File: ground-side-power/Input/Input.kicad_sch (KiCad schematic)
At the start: 35 parts, among them J1 Battery Terminals, J2 Battery Terminals, J3 Battery Terminals, J4 Battery Terminals, J5 455860005, J6 455860005, J7 ATX-24, J8 Conn_01x03_Female, J9 Conn_01x03_Female, K1 AZ2150-1A-12DEF, SW1 GRB234A2NABA1, U1 INA180, U2 INA180

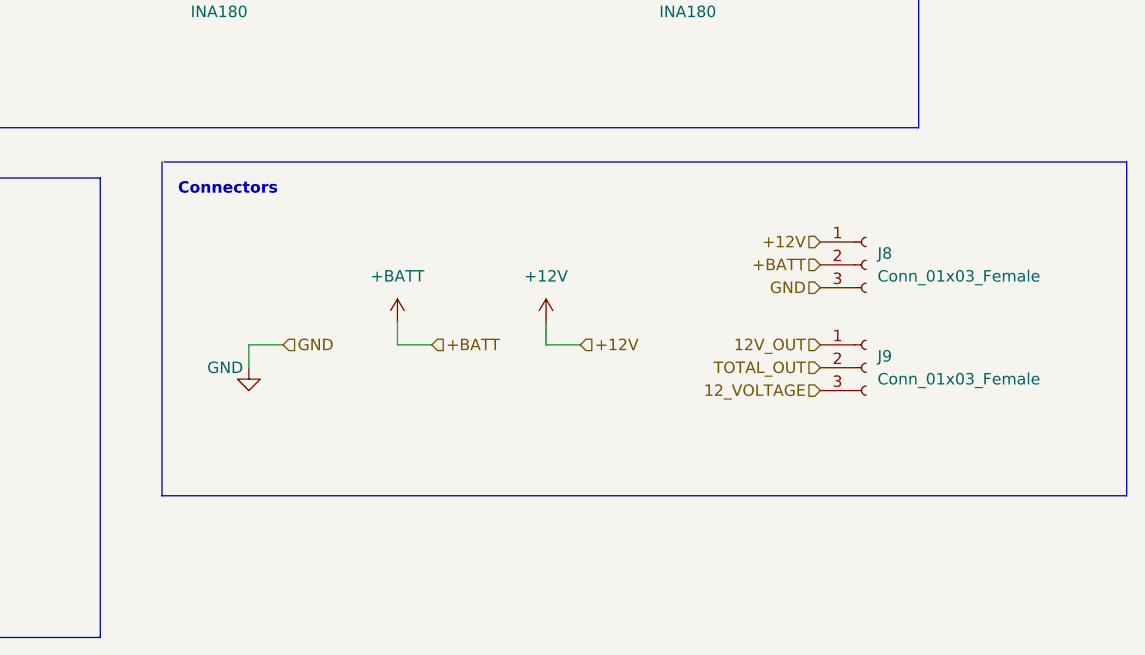
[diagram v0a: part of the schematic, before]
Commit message: Created layout for the footprints for each board
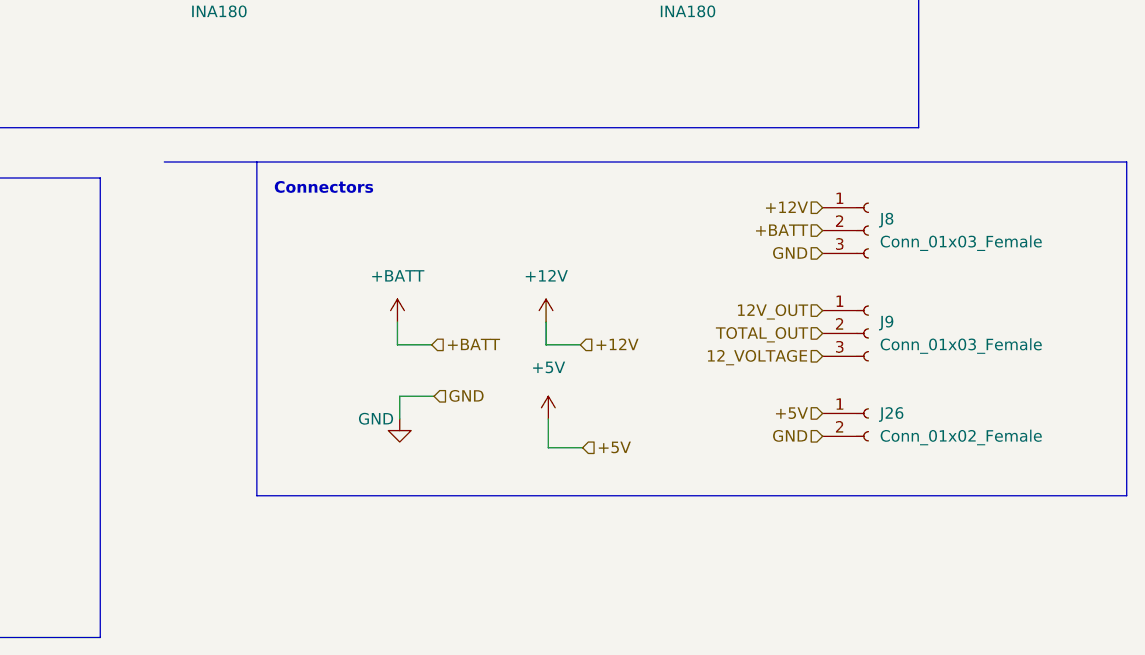
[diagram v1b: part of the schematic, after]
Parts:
- added J26: Conn_01x02_Female, GSP:OSTTA020161, symbol Connector:Conn_01x02_Female
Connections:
- net +5V: now also J26.1 (Pin_1)
- net GND: now also J26.2 (Pin_2)
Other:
- moved on the sheet: J8, J9
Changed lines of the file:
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@@
     (stroke (width 0) (type default) (color 0 0 0 0))
   )
-  (wire (pts (xy 183.896 146.05) (xy 187.706 146.05))
+  (wire (pts (xy 200.66 151.765) (xy 204.47 151.765))
     (stroke (width 0) (type default) (color 0 0 0 0))
   )
@@
     (stroke (width 0) (type default) (color 0 0 0 0))
   )
+  (wire (pts (xy 220.98 157.48) (xy 217.17 157.48))
+    (stroke (width 0) (type default) (color 0 0 0 0))
+  )
   (wire (pts (xy 62.611 31.242) (xy 62.611 32.512))
     (stroke (width 0) (type default) (color 0 0 0 0))
@@
     (stroke (width 0) (type default) (color 0 0 0 0))
   )
-  (polyline (pts (xy 281.432 162.814) (xy 174.244 162.814))
+  (polyline (pts (xy 281.432 162.814) (xy 184.785 162.814))
     (stroke (width 0) (type default) (color 0 0 0 0))
   )
@@
     (stroke (width 0) (type default) (color 0 0 0 0))
   )
-  (polyline (pts (xy 174.244 162.814) (xy 174.244 125.73))
+  (polyline (pts (xy 184.785 162.814) (xy 184.785 125.73))
     (stroke (width 0) (type default) (color 0 0 0 0))
   )
@@
     (stroke (width 0) (type default) (color 0 0 0 0))
   )
-  (wire (pts (xy 183.896 148.59) (xy 183.896 146.05))
+  (wire (pts (xy 200.66 154.305) (xy 200.66 151.765))
     (stroke (width 0) (type default) (color 0 0 0 0))
   )
@@
   )
   (wire (pts (xy 95.631 157.861) (xy 95.631 161.036))
+    (stroke (width 0) (type default) (color 0 0 0 0))
+  )
+  (wire (pts (xy 217.17 154.305) (xy 217.17 157.48))
     (stroke (width 0) (type default) (color 0 0 0 0))
   )
@@
     (effects (font (size 1.27 1.27)) (justify left bottom))
   )
-  (text "Connectors" (at 176.022 129.54 0)
+  (text "Connectors" (at 186.69 129.54 0)
     (effects (font (size 1.27 1.27) bold) (justify left bottom))
   )
@@
     (effects (font (size 1.27 1.27)) (justify left))
   )
-  (hierarchical_label "12V_OUT" (shape input) (at 247.396 146.05 180)
+  (hierarchical_label "12V_OUT" (shape input) (at 247.65 142.24 180)
     (effects (font (size 1.27 1.27)) (justify right))
   )
-  (hierarchical_label "TOTAL_OUT" (shape input) (at 247.396 148.59 180)
+  (hierarchical_label "TOTAL_OUT" (shape input) (at 247.65 144.78 180)
     (effects (font (size 1.27 1.27)) (justify right))
   )
-  (hierarchical_label "12_VOLTAGE" (shape input) (at 247.396 151.13 180)
+  (hierarchical_label "12_VOLTAGE" (shape input) (at 247.65 147.32 180)
     (effects (font (size 1.27 1.27)) (justify right))
   )
@@
     (effects (font (size 1.27 1.27)) (justify left))
   )
-  (hierarchical_label "GND" (shape input) (at 187.706 146.05 0)
+  (hierarchical_label "GND" (shape input) (at 204.47 151.765 0)
     (effects (font (size 1.27 1.27)) (justify left))
   )
@@
     (effects (font (size 1.27 1.27)) (justify left))
   )
-  (hierarchical_label "GND" (shape input) (at 247.396 139.7 180)
+  (hierarchical_label "GND" (shape input) (at 247.65 135.89 180)
     (effects (font (size 1.27 1.27)) (justify right))
   )
-  (hierarchical_label "+12V" (shape input) (at 247.396 134.62 180)
+  (hierarchical_label "GND" (shape input) (at 247.65 156.21 180)
+    (effects (font (size 1.27 1.27)) (justify right))
+  )
+  (hierarchical_label "+12V" (shape input) (at 247.65 130.81 180)
     (effects (font (size 1.27 1.27)) (justify right))
   )
@@
     (effects (font (size 1.27 1.27)) (justify left))
   )
-  (hierarchical_label "+BATT" (shape input) (at 247.396 137.16 180)
+  (hierarchical_label "+5V" (shape input) (at 247.65 153.67 180)
+    (effects (font (size 1.27 1.27)) (justify right))
+  )
+  (hierarchical_label "+5V" (shape input) (at 220.98 157.48 0)
+    (effects (font (size 1.27 1.27)) (justify left))
+  )
+  (hierarchical_label "+BATT" (shape input) (at 247.65 133.35 180)
     (effects (font (size 1.27 1.27)) (justify right))
   )
@@
     )
     (property "Datasheet" "" (id 3) (at 221.996 33.782 0)
+      (effects (font (size 1.27 1.27)) hide)
+    )
+    (pin "1")
+  )
+  (symbol (lib_id "power:+5V") (at 217.17 154.305 0) (unit 1)
+    (in_bom yes) (on_board yes) (fields_autoplaced)
+    (property "Reference" "#PWR0103" (id 0) (at 217.17 158.115 0)
+      (effects (font (size 1.27 1.27)) hide)
+    )
+    (property "Value" "+5V" (id 1) (at 217.17 148.59 0))
+    (property "Footprint" "" (id 2) (at 217.17 154.305 0)
+      (effects (font (size 1.27 1.27)) hide)
+    )
+    (property "Datasheet" "" (id 3) (at 217.17 154.305 0)
       (effects (font (size 1.27 1.27)) hide)
     )
@@
     (pin "9")
   )
+  (symbol (lib_id "Connector:Conn_01x02_Female") (at 252.73 153.67 0) (unit 1)
+    (in_bom yes) (on_board yes) (fields_autoplaced)
+    (property "Reference" "J26" (id 0) (at 254 153.6699 0)
+      (effects (font (size 1.27 1.27)) (justify left))
+    )
+    (property "Value" "Conn_01x02_Female" (id 1) (at 254 156.2099 0)
+      (effects (font (size 1.27 1.27)) (justify left))
+    )
+    (property "Footprint" "GSP:OSTTA020161" (id 2) (at 252.73 153.67 0)
+      (effects (font (size 1.27 1.27)) hide)
+    )
+    (property "Datasheet" "~" (id 3) (at 252.73 153.67 0)
+      (effects (font (size 1.27 1.27)) hide)
+    )
+    (pin "1")
+    (pin "2")
+  )
   (symbol (lib_id "Device:R_Small_US") (at 250.825 50.292 0) (mirror x) (unit 1)
     (in_bom yes) (on_board yes) (fields_autoplaced)
@@
     (pin "8")
   )
-  (symbol (lib_id "power:GND") (at 183.896 148.59 0) (mirror y) (unit 1)
-    (in_bom yes) (on_board yes)
-    (property "Reference" "#PWR028" (id 0) (at 183.896 154.94 0)
-      (effects (font (size 1.27 1.27)) hide)
-    )
-    (property "Value" "GND" (id 1) (at 183.261 148.59 0)
-      (effects (font (size 1.27 1.27)) (justify left))
-    )
-    (property "Footprint" "" (id 2) (at 183.896 148.59 0)
-      (effects (font (size 1.27 1.27)) hide)
-    )
-    (property "Datasheet" "" (id 3) (at 183.896 148.59 0)
+  (symbol (lib_id "power:GND") (at 200.66 154.305 0) (mirror y) (unit 1)
+    (in_bom yes) (on_board yes)
+    (property "Reference" "#PWR028" (id 0) (at 200.66 160.655 0)
+      (effects (font (size 1.27 1.27)) hide)
+    )
+    (property "Value" "GND" (id 1) (at 200.025 154.305 0)
+      (effects (font (size 1.27 1.27)) (justify left))
+    )
+    (property "Footprint" "" (id 2) (at 200.66 154.305 0)
+      (effects (font (size 1.27 1.27)) hide)
+    )
+    (property "Datasheet" "" (id 3) (at 200.66 154.305 0)
       (effects (font (size 1.27 1.27)) hide)
     )
@@
     (pin "1")
   )
-  (symbol (lib_id "Connector:Conn_01x03_Female") (at 252.476 148.59 0) (unit 1)
-    (in_bom yes) (on_board yes) (fields_autoplaced)
-    (property "Reference" "J9" (id 0) (at 253.746 147.3199 0)
-      (effects (font (size 1.27 1.27)) (justify left))
-    )
-    (property "Value" "Conn_01x03_Female" (id 1) (at 253.746 149.8599 0)
-      (effects (font (size 1.27 1.27)) (justify left))
-    )
-    (property "Footprint" "GSP:TB005-762-03BE" (id 2) (at 252.476 148.59 0)
-      (effects (font (size 1.27 1.27)) hide)
-    )
-    (property "Datasheet" "~" (id 3) (at 252.476 148.59 0)
+  (symbol (lib_id "Connector:Conn_01x03_Female") (at 252.73 144.78 0) (unit 1)
+    (in_bom yes) (on_board yes) (fields_autoplaced)
+    (property "Reference" "J9" (id 0) (at 254 143.5099 0)
+      (effects (font (size 1.27 1.27)) (justify left))
+    )
+    (property "Value" "Conn_01x03_Female" (id 1) (at 254 146.0499 0)
+      (effects (font (size 1.27 1.27)) (justify left))
+    )
+    (property "Footprint" "GSP:TB005-762-03BE" (id 2) (at 252.73 144.78 0)
+      (effects (font (size 1.27 1.27)) hide)
+    )
+    (property "Datasheet" "~" (id 3) (at 252.73 144.78 0)
       (effects (font (size 1.27 1.27)) hide)
     )
@@
     (pin "2")
   )
-  (symbol (lib_id "Connector:Conn_01x03_Female") (at 252.476 137.16 0) (unit 1)
-    (in_bom yes) (on_board yes) (fields_autoplaced)
-    (property "Reference" "J8" (id 0) (at 253.746 135.8899 0)
-      (effects (font (size 1.27 1.27)) (justify left))
-    )
-    (property "Value" "Conn_01x03_Female" (id 1) (at 253.746 138.4299 0)
-      (effects (font (size 1.27 1.27)) (justify left))
-    )
-    (property "Footprint" "GSP:TB005-762-03BE" (id 2) (at 252.476 137.16 0)
-      (effects (font (size 1.27 1.27)) hide)
-    )
-    (property "Datasheet" "~" (id 3) (at 252.476 137.16 0)
-      (effects (font (size 1.27 1.27)) hide)
-    )
+  (symbol (lib_id "Connector:Conn_01x03_Female") (at 252.73 133.35 0) (unit 1)
+    (in_bom yes) (on_board yes) (fields_autoplaced)
+    (property "Reference" "J8" (id 0) (at 254 132.0799 0)
+      (effects (font (size 1.27 1.27)) (justify left))
+    )
+    (property "Value" "Conn_01x03_Female" (id 1) (at 254 134.6199 0)
+      (effects (font (size 1.27 1.27)) (justify left))
+    )
+    (property "Footprint" "GSP:TB005-762-03BE" (id 2) (at 252.73 133.35 0)
+      (effects (font (size 1.27 1.27)) hide)
+    )
+    (property "Datasheet" "~" (id 3) (at 252.73 133.35 0)
+      (effects (font (size 1.27 1.27)) hide)
+    )

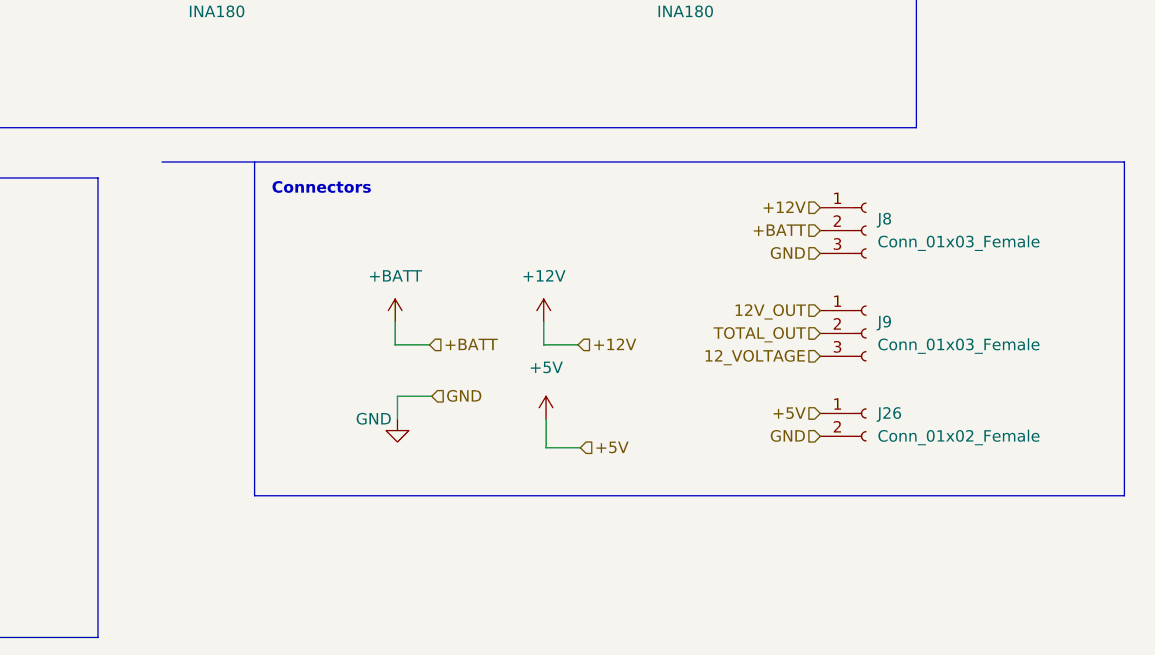
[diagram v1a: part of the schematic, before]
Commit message: Added Fan Headers + Thermistor
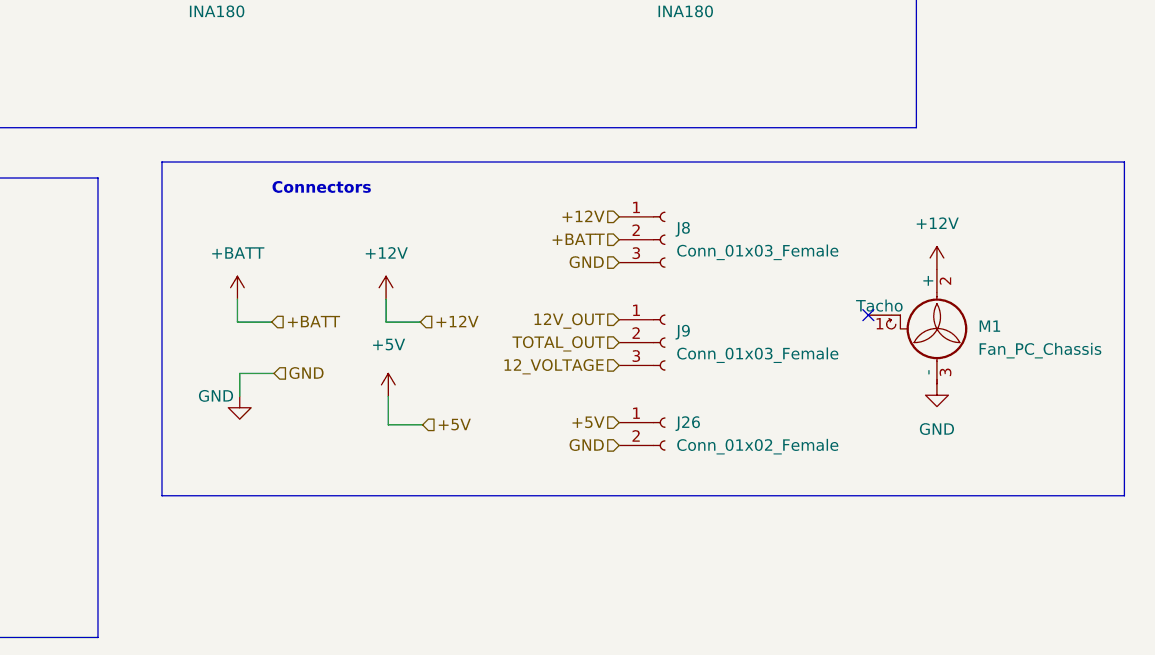
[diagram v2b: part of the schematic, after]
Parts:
- added M1: Fan_PC_Chassis, Connector:FanPinHeader_1x03_P2.54mm_Vertical, symbol Motor:Fan_PC_Chassis
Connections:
- net +12V: now also M1.2 (+)
- net GND: now also M1.3 (-)
- no-connect marks 6 -> 7
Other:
- moved on the sheet: J26, J8, J9
